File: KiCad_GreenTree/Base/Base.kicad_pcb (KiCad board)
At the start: 2 copper layers, 100 x 100 mm, 23 parts, among them Q1 BCX56, Q2 BCX56, Q3 BCX56, Q4 BCX56, SW1 SW_DPDT_x2, U1 NE555D, U2 NE555D, U3 74HC04, U4 74HC04

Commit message: Verbindung zu Baum
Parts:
- removed U4: 74HC04, Package_SO:SOIC-14W_7.5x9mm_P1.27mm
- added REF**: Verbindung_Basis, Bib:Verbindung_Basis, F.Cu at (137.1, 92.4)
- C1: footprint Capacitor_SMD:C_01005_0402Metric -> Capacitor_SMD:C_1206_3216Metric_Pad1.33x1.80mm_HandSolder
- C2, C3, C4: footprint Capacitor_SMD:C_01005_0402Metric_Pad0.57x0.30mm_HandSolder -> Capacitor_SMD:C_1206_3216Metric_Pad1.33x1.80mm_HandSolder
- R1, R2, R3, R4, R5, R6: footprint Resistor_SMD:R_01005_0402Metric_Pad0.57x0.30mm_HandSolder -> Resistor_SMD:R_1206_3216Metric_Pad1.30x1.75mm_HandSolder
- moved C3 28.0 mm to (71.1, 85.5)
- moved C4 28.0 mm to (68.5, 85.5)
- moved R1 28.0 mm to (74.3, 85.9)
- moved R2 28.0 mm to (65.9, 84.2)
- moved R4 28.0 mm to (73.7, 84.2)
- moved R5 28.0 mm to (76.3, 84.2)
- moved R6 28.0 mm to (76.9, 85.9)
- moved C2 28.0 mm to (68.5, 83.8)
- moved R3 28.0 mm to (71.1, 83.8)
- moved U1 25.0 mm to (45.0, 70.4)
- moved BT1 19.2 mm to (183.4, 103.3)
- moved BT4 19.2 mm to (125.0, 139.3)
- moved C1 18.6 mm to (66.3, 78.7)
- moved U3 18.3 mm to (55.6, 121.9)
- moved Q2 15.2 mm to (37.8, 105.9)
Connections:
- U3 pad 3: (no net) -> Net-(Q2-Pad1)
- U3 pad 4: (no net) -> Net-(Q4-Pad1)
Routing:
- net Net-(BT1-Pad1): track 19.6 -> 0.00 mm
- net Net-(BT1-Pad2): track 19.9 -> 0.31 mm
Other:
- board text added: "+"
- board text added: "-"

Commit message: NE555 Layout
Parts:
- added C5: 100n, Capacitor_SMD:C_1206_3216Metric_Pad1.33x1.80mm_HandSolder, B.Cu at (58.9, 65.3)
- added C6: 100n, Capacitor_SMD:C_1206_3216Metric_Pad1.33x1.80mm_HandSolder, B.Cu at (59.4, 76.7)
- SW1: footprint Button_Switch_THT:SW_E-Switch_EG2219_DPDT_Angled -> Bib:Schiebeschalter
- moved SW1 81.6 mm to (173.5, 66.8), turned to 90 degrees
- moved BT3 78.2 mm to (107.2, 64.0), turned to 0 degrees
- moved BT1 77.7 mm to (106.9, 116.8), turned to 0 degrees
- moved BT4 44.2 mm to (165.1, 120.9), turned to 180 degrees
- moved U3 43.0 mm to (95.8, 106.4), turned to 270 degrees
- moved BT2 42.1 mm to (165.3, 67.8), turned to 180 degrees
- moved Q2 38.4 mm to (75.9, 101.1), turned to 270 degrees
- moved U2 37.0 mm to (58.7, 69.6), turned to 180 degrees
- moved R4 28.3 mm to (51.1, 67.3), turned to 270 degrees
- moved Q4 27.3 mm to (81.5, 101.1), turned to 270 degrees
- moved R6 26.4 mm to (70.9, 111.5), turned to 180 degrees
- moved R3 24.0 mm to (53.6, 67.3), turned to 270 degrees
- moved Q1 23.6 mm to (76.5, 113.0), turned to 270 degrees
- moved R1 21.9 mm to (53.6, 78.7), turned to 270 degrees
- moved C4 21.2 mm to (51.1, 73.4), turned to 270 degrees
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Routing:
- net GND: track 0.00 -> 38.8 mm
- net Net-(BT1-Pad1): track 0.00 -> 32.8 mm
- net Net-(BT1-Pad2): track 0.31 -> 20.4 mm
- net Net-(C4-Pad1): track 0.00 -> 13.5 mm
- net Net-(C3-Pad1): track 0.00 -> 13.5 mm
- net VCC: track 0.00 -> 12.1 mm
- net Net-(BT3-Pad1): track 0.00 -> 11.6 mm
- net Net-(R3-Pad2): track 0.00 -> 7.71 mm
- net Net-(R1-Pad2): track 0.00 -> 7.65 mm
- net Net-(C1-Pad1): track 0.00 -> 2.90 mm
- net Net-(BT2-Pad1): track 18.3 -> 20.2 mm
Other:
- board text removed: "+"
- board text removed: "-"

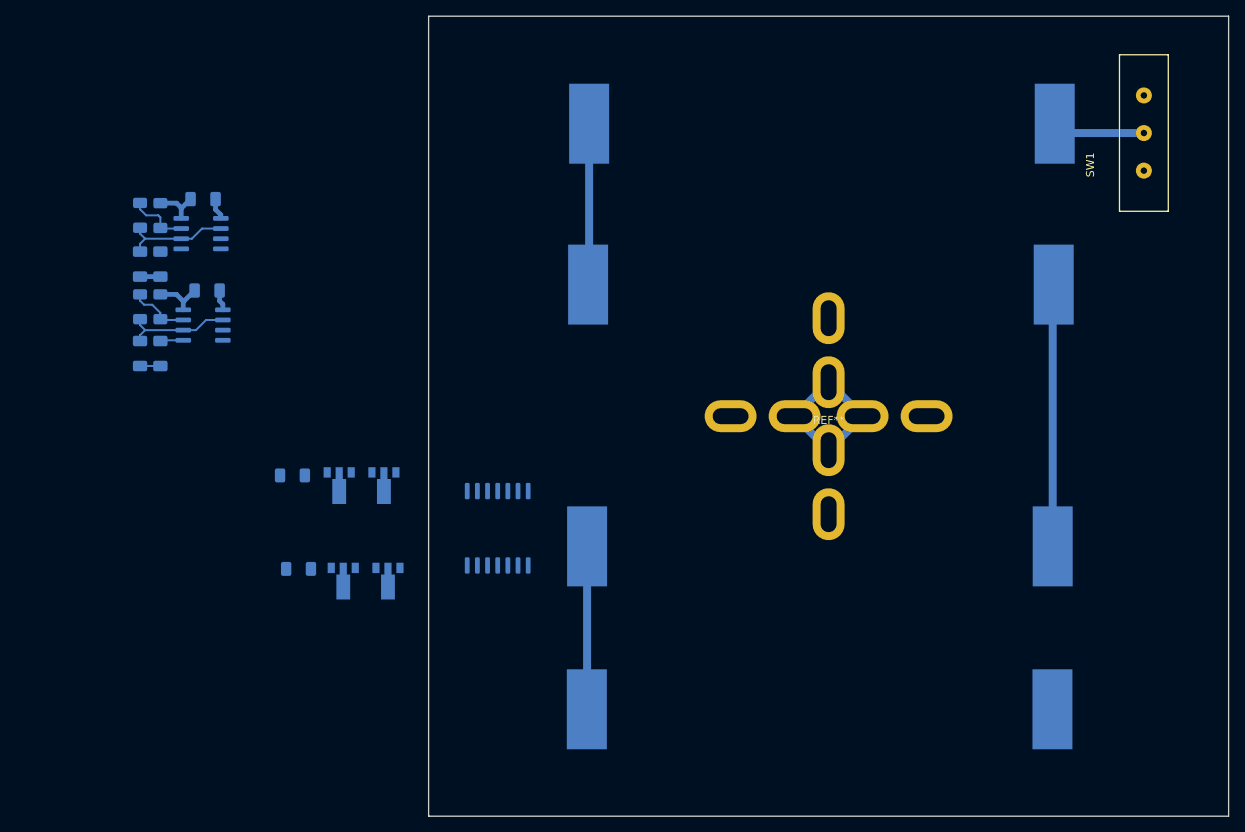
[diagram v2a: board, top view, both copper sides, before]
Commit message: Without GND
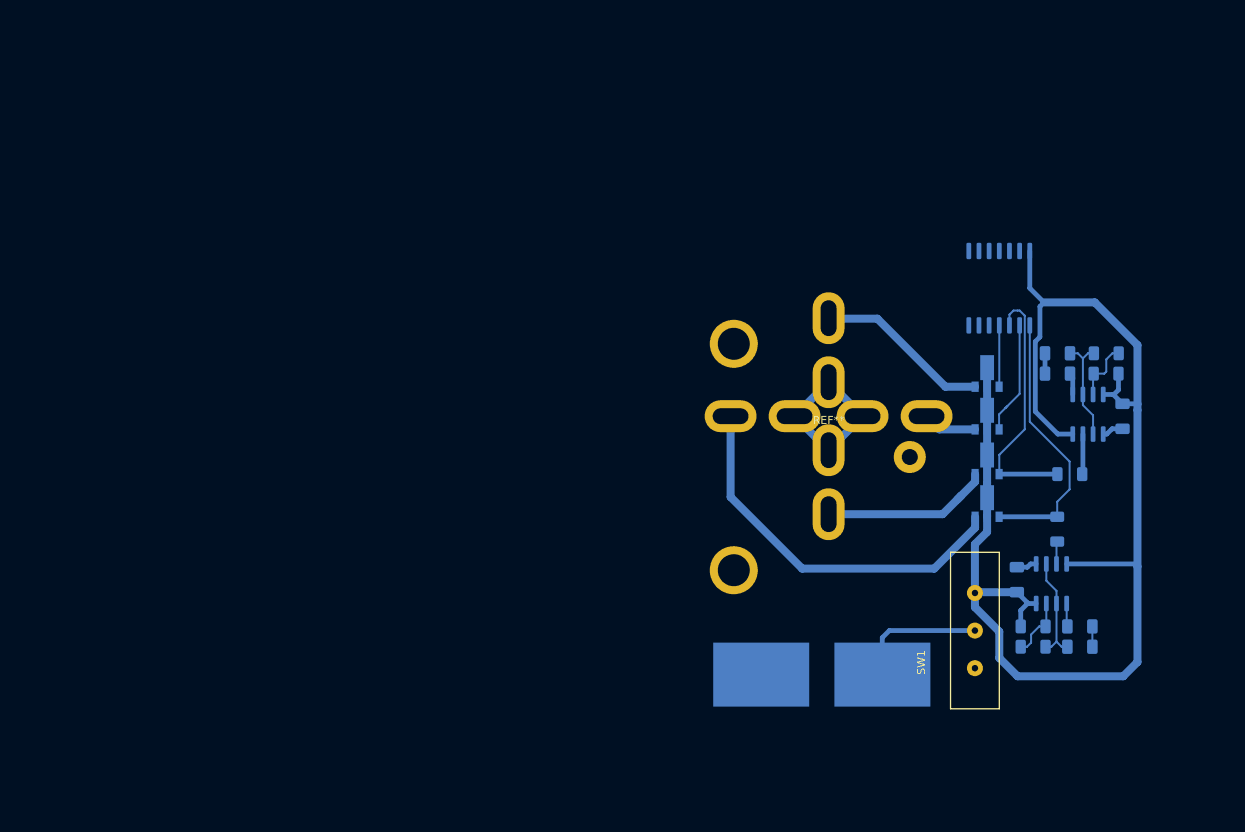
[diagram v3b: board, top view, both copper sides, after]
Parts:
- removed BT1, BT2, BT4: 1.5, Bib:Batteriehalter_für_1_Mignonzelle(AA)
- BT3: value 1.5 -> 9V; footprint Bib:Batteriehalter_für_1_Mignonzelle(AA) -> Bib:9V_Holder
- moved C3 123.1 mm to (168.5, 121.2), turned to 0 degrees
- moved R4 122.0 mm to (171.8, 84.6), turned to 180 degrees
- moved C1 119.9 mm to (168.5, 118.7), turned to 0 degrees
- moved R3 119.9 mm to (171.8, 87.1), turned to 180 degrees
- moved R2 119.4 mm to (162.7, 121.2), turned to 0 degrees
- moved C5 118.1 mm to (173.9, 92.4), turned to 270 degrees
- moved R1 116.2 mm to (162.7, 118.7), turned to 0 degrees
- moved C4 115.2 mm to (165.7, 84.6), turned to 180 degrees
- moved U2 113.1 mm to (169.5, 92.2), turned to 90 degrees
- moved C2 113.0 mm to (165.7, 87.1), turned to 180 degrees
- moved U1 110.9 mm to (165.0, 113.4), turned to 270 degrees
- moved C6 107.5 mm to (160.7, 112.9), turned to 90 degrees
- moved R5 97.2 mm to (167.3, 99.7), turned to 0 degrees
- moved R6 95.0 mm to (165.7, 106.5), turned to 270 degrees
- moved Q1 81.1 mm to (156.9, 103.3), turned to 90 degrees
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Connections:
- BT3 pad 2: Net-(BT2-Pad1) -> GND
- REF** pad 2: (no net) -> /LED_MATRIX_4
- REF** pad 4: (no net) -> /LED_MATRIX_2
- REF** pad 6: (no net) -> /LED_MATRIX_3
- REF** pad 8: (no net) -> /LED_MATRIX_1
- U3 pad 14: (no net) -> VCC
- U3 pad 7: (no net) -> GND
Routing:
- net VCC: track 12.1 -> 166.5 mm
- net /LED_MATRIX_1: track 0.00 -> 47.9 mm
- net Net-(Q1-Pad1): track 0.00 -> 33.7 mm
- net Net-(BT1-Pad1): track 32.8 -> 0.00 mm
- net Net-(Q2-Pad1): track 0.00 -> 32.0 mm
- net /LED_MATRIX_4: track 0.00 -> 21.8 mm
- net /LED_MATRIX_3: track 0.00 -> 21.6 mm
- net Net-(BT1-Pad2): track 20.4 -> 0.00 mm
- net Net-(BT2-Pad1): track 20.2 -> 0.00 mm
- net Net-(Q3-Pad1): track 0.00 -> 14.4 mm
- net Net-(Q4-Pad1): track 0.00 -> 7.80 mm
- net /LED_MATRIX_2: track 0.00 -> 6.78 mm
- net Net-(R5-Pad2): track 0.00 -> 5.04 mm
- net Net-(BT3-Pad1): track 11.6 -> 16.6 mm
- net GND: track 38.8 -> 34.4 mm
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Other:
- board outline removed
- net class VCC: clearance 0.4 -> 0.25

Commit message: Entwurf1
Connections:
- REF** pad 4: /LED_MATRIX_2 -> /LED_MATRIX_3
- REF** pad 6: /LED_MATRIX_3 -> /LED_MATRIX_2
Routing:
- net GND: track 34.4 -> 217.7 mm, vias 0 -> 6
- net /LED_MATRIX_2: track 6.78 -> 31.7 mm
- net /LED_MATRIX_3: track 21.6 -> 11.3 mm
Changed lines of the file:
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@@
     (thickness 1.6)
     (drawings 0)
-    (tracks 131)
+    (tracks 188)
     (zones 0)
     (modules 22)
@@
     )
     (pad 6 thru_hole oval (at 0 12.25) (size 4 6.5) (drill oval 2 4.5) (layers *.Cu *.Mask)
-      (net 10 /LED_MATRIX_3))
+      (net 12 /LED_MATRIX_2))
     (pad 5 thru_hole oval (at 0 4.25) (size 4 6.5) (drill oval 2 4.5) (layers *.Cu *.Mask)
       (net 2 GND))
@@
       (net 2 GND))
     (pad 4 thru_hole oval (at 12.25 0) (size 6.5 4) (drill oval 4.5 2) (layers *.Cu *.Mask)
-      (net 12 /LED_MATRIX_2))
+      (net 10 /LED_MATRIX_3))
     (pad 3 thru_hole oval (at 4.25 0) (size 6.5 4) (drill oval 4.5 2) (layers *.Cu *.Mask)
       (net 2 GND))
@@
   (segment (start 172.5547 93.9931) (end 173.8632 93.9931) (width 0.6) (layer B.Cu) (net 2))
   (segment (start 171.8962 94.6516) (end 172.5547 93.9931) (width 0.6) (layer B.Cu) (net 2))
+  (segment (start 170.0915 118.6944) (end 170.0915 114.4655) (width 1) (layer B.Cu) (net 2))
+  (via (at 166.586 112.992) (size 0.8) (drill 0.4) (layers F.Cu B.Cu) (net 2))
+  (segment (start 168.618 112.992) (end 166.586 112.992) (width 1) (layer B.Cu) (net 2))
+  (segment (start 170.0915 114.4655) (end 168.618 112.992) (width 1) (layer B.Cu) (net 2))
+  (via (at 163.284 112.992) (size 0.8) (drill 0.4) (layers F.Cu B.Cu) (net 2))
+  (segment (start 166.586 112.992) (end 163.284 112.992) (width 1) (layer F.Cu) (net 2))
+  (segment (start 163.284 112.992) (end 162.522 112.992) (width 1) (layer B.Cu) (net 2))
+  (segment (start 162.522 112.992) (end 160.998 111.468) (width 1) (layer B.Cu) (net 2))
+  (segment (start 160.655 107.747) (end 162.014 106.388) (width 1) (layer B.Cu) (net 2))
+  (segment (start 160.655 111.2899) (end 160.655 107.747) (width 1) (layer B.Cu) (net 2))
+  (segment (start 173.952 100.292) (end 173.952 93.942) (width 1) (layer B.Cu) (net 2))
+  (via (at 171.412 92.418) (size 0.8) (drill 0.4) (layers F.Cu B.Cu) (net 2))
+  (segment (start 171.4502 92.4562) (end 171.412 92.418) (width 1) (layer B.Cu) (net 2))
+  (segment (start 171.4502 94.6516) (end 171.4502 92.4562) (width 1) (layer B.Cu) (net 2))
+  (via (at 168.11 92.418) (size 0.8) (drill 0.4) (layers F.Cu B.Cu) (net 2))
+  (segment (start 171.412 92.418) (end 168.11 92.418) (width 1) (layer F.Cu) (net 2))
+  (segment (start 168.11 92.418) (end 164.046 88.354) (width 1) (layer B.Cu) (net 2))
+  (segment (start 164.046 87.592) (end 164.3 87.338) (width 1) (layer B.Cu) (net 2))
+  (segment (start 164.046 88.354) (end 164.046 87.592) (width 1) (layer B.Cu) (net 2))
+  (segment (start 165.57 83.1593) (end 165.57 79.972) (width 1) (layer B.Cu) (net 2))
+  (segment (start 164.1727 84.5566) (end 165.57 83.1593) (width 1) (layer B.Cu) (net 2))
+  (segment (start 154.648 81.066) (end 154.648 79.914315) (width 1) (layer B.Cu) (net 2))
+  (segment (start 154.648 79.914315) (end 154.590315 79.914315) (width 1) (layer B.Cu) (net 2))
+  (segment (start 154.590315 79.914315) (end 149.568 74.892) (width 1) (layer B.Cu) (net 2))
+  (segment (start 149.568 74.892) (end 137.32961 74.892) (width 1) (layer B.Cu) (net 2))
+  (segment (start 137.32961 74.892) (end 134.328 74.892) (width 1) (layer B.Cu) (net 2))
+  (segment (start 134.328 74.892) (end 130.772 78.448) (width 1) (layer B.Cu) (net 2))
+  (segment (start 130.772 78.448) (end 130.772 82.004) (width 1) (layer B.Cu) (net 2))
+  (segment (start 130.772 82.004) (end 137.122 88.354) (width 1) (layer B.Cu) (net 2))
+  (segment (start 128.695 124.72) (end 128.95 124.72) (width 1) (layer B.Cu) (net 2))
+  (segment (start 128.95 124.72) (end 131.28 122.39) (width 1) (layer B.Cu) (net 2))
+  (segment (start 131.28 112.203998) (end 123.152 104.075998) (width 1) (layer B.Cu) (net 2))
+  (segment (start 131.28 122.39) (end 131.28 112.203998) (width 1) (layer B.Cu) (net 2))
+  (segment (start 120.92199 91.29962) (end 123.86761 88.354) (width 1) (layer B.Cu) (net 2))
+  (segment (start 120.92199 101.845988) (end 120.92199 91.29962) (width 1) (layer B.Cu) (net 2))
+  (segment (start 123.152 104.075998) (end 120.92199 101.845988) (width 1) (layer B.Cu) (net 2))
+  (segment (start 123.86761 88.354) (end 136.868 88.354) (width 1) (layer B.Cu) (net 2))
+  (segment (start 167.856 106.388) (end 173.952 100.292) (width 1) (layer B.Cu) (net 2))
+  (segment (start 162.014 106.388) (end 167.856 106.388) (width 1) (layer B.Cu) (net 2))
+  (via (at 165.57 79.464) (size 0.8) (drill 0.4) (layers F.Cu B.Cu) (net 2))
+  (segment (start 165.57 79.972) (end 165.57 79.464) (width 1) (layer B.Cu) (net 2))
+  (via (at 165.57 76.924) (size 0.8) (drill 0.4) (layers F.Cu B.Cu) (net 2))
+  (segment (start 165.57 79.464) (end 165.57 76.924) (width 1) (layer F.Cu) (net 2))
+  (segment (start 149.568 74.618902) (end 149.568 74.892) (width 1) (layer B.Cu) (net 2))
+  (segment (start 154.374902 69.812) (end 149.568 74.618902) (width 1) (layer B.Cu) (net 2))
+  (segment (start 164.3 69.812) (end 154.374902 69.812) (width 1) (layer B.Cu) (net 2))
+  (segment (start 165.57 71.082) (end 164.3 69.812) (width 1) (layer B.Cu) (net 2))
+  (segment (start 165.57 76.924) (end 165.57 71.082) (width 1) (layer B.Cu) (net 2))
   (segment (start 166.878 118.6059) (end 166.9665 118.6944) (width 0.25) (layer B.Cu) (net 3))
   (segment (start 166.878 115.8354) (end 166.878 118.6059) (width 0.25) (layer B.Cu) (net 3))
@@
   (segment (start 162.268 93.1038) (end 167.2464 98.0822) (width 0.25) (layer B.Cu) (net 9))
   (segment (start 162.268 81.066) (end 162.268 93.1038) (width 0.25) (layer B.Cu) (net 9))
-  (segment (start 155.434 99.656) (end 155.434 100.612824) (width 1) (layer B.Cu) (net 10))
-  (segment (start 151.378824 104.668) (end 153.677412 102.369412) (width 1) (layer B.Cu) (net 10))
-  (segment (start 137.122 104.668) (end 151.378824 104.668) (width 1) (layer B.Cu) (net 10))
-  (segment (start 153.677412 102.369412) (end 153.214824 102.832) (width 1) (layer B.Cu) (net 10))
-  (segment (start 155.434 100.612824) (end 153.677412 102.369412) (width 1) (layer B.Cu) (net 10))
   (segment (start 158.434 99.656) (end 165.4928 99.656) (width 0.6) (layer B.Cu) (net 11))
   (segment (start 159.728 81.066) (end 159.728 79.718) (width 0.25) (layer B.Cu) (net 11))
@@
   (segment (start 161.64299 94.05901) (end 158.458 97.244) (width 0.25) (layer B.Cu) (net 11))
   (segment (start 158.458 97.244) (end 158.458 99.784) (width 0.25) (layer B.Cu) (net 11))
-  (segment (start 155.434 94.068) (end 150.964 94.068) (width 1) (layer B.Cu) (net 12))
-  (segment (start 149.372 92.476) (end 150.964 94.068) (width 1) (layer B.Cu) (net 12))
-  (segment (start 149.372 92.418) (end 149.372 92.476) (width 1) (layer B.Cu) (net 12))
+  (segment (start 149.372 92.418) (end 149.372 92.476) (width 1) (layer B.Cu) (net 10))
+  (segment (start 155.434 99.656) (end 152.996 99.656) (width 1) (layer B.Cu) (net 10))
+  (segment (start 152.996 99.656) (end 149.822 96.482) (width 1) (layer B.Cu) (net 10))
+  (segment (start 149.822 96.482) (end 149.822 94.704) (width 1) (layer B.Cu) (net 10))
+  (segment (start 149.822 94.704) (end 149.822 92.164) (width 1) (layer B.Cu) (net 10))
+  (segment (start 137.122 104.668) (end 139.35 104.668) (width 1) (layer B.Cu) (net 12))
+  (segment (start 139.35 104.668) (end 140.62 104.668) (width 1) (layer B.Cu) (net 12))
+  (segment (start 140.62 104.668) (end 143.726 101.562) (width 1) (layer B.Cu) (net 12))
+  (segment (start 143.726 97.067998) (end 143.726 101.562) (width 1) (layer B.Cu) (net 12))
+  (segment (start 145.32201 95.471988) (end 143.726 97.067998) (width 1) (layer B.Cu) (net 12))
+  (segment (start 145.32201 91.32999) (end 145.32201 95.471988) (width 1) (layer B.Cu) (net 12))
+  (segment (start 146.93401 89.71799) (end 145.32201 91.32999) (width 1) (layer B.Cu) (net 12))
+  (segment (start 151.74038 89.71799) (end 146.93401 89.71799) (width 1) (layer B.Cu) (net 12))
+  (segment (start 153.32201 91.29962) (end 151.74038 89.71799) (width 1) (layer B.Cu) (net 12))
+  (segment (start 153.32201 91.95601) (end 153.32201 91.29962) (width 1) (layer B.Cu) (net 12))
+  (segment (start 155.434 94.068) (end 153.32201 91.95601) (width 1) (layer B.Cu) (net 12))
   (segment (start 158.434 94.068) (end 158.434 92.188) (width 0.25) (layer B.Cu) (net 13))
   (segment (start 158.434 92.188) (end 159.22 91.402) (width 0.25) (layer B.Cu) (net 13))
@@
   (segment (start 160.998 81.066) (end 160.998 89.624) (width 0.25) (layer B.Cu) (net 13))
   (segment (start 159.22 91.402) (end 159.474 91.148) (width 0.25) (layer B.Cu) (net 13))
-  (segment (start 155.434 88.734) (end 151.726 88.734) (width 1) (layer B.Cu) (net 14))
-  (segment (start 151.726 88.734) (end 143.218 80.226) (width 1) (layer B.Cu) (net 14))
   (segment (start 143.218 80.226) (end 137.122 80.226) (width 1) (layer B.Cu) (net 14))
+  (segment (start 155.434 88.734) (end 153.25 88.734) (width 1) (layer B.Cu) (net 14))
+  (segment (start 144.742 80.226) (end 143.218 80.226) (width 1) (layer B.Cu) (net 14))
+  (segment (start 153.25 88.734) (end 144.742 80.226) (width 1) (layer B.Cu) (net 14))
   (segment (start 158.458 81.066) (end 158.458 88.862) (width 0.25) (layer B.Cu) (net 15))
   (segment (start 164.237 118.6944) (end 163.449 118.6944) (width 0.25) (layer B.Cu) (net 16))

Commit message: update
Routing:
- added copper zone on B.Cu, net GND
- added copper zone on F.Cu, net GND
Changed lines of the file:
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@@
       (effects (font (size 1 1) (thickness 0.15)) (justify mirror))
     )
-    (fp_text value 9V (at 27.325 1.425 90) (layer B.Fab)
+    (fp_text value 9V (at 27.432 -1.27 90) (layer B.Fab)
       (effects (font (size 1 1) (thickness 0.15)) (justify mirror))
     )
@@
   (segment (start 168.9102 94.6516) (end 168.9102 99.695) (width 0.6) (layer B.Cu) (net 18))
   (segment (start 165.608 110.8854) (end 165.608 108.1534) (width 0.25) (layer B.Cu) (net 19))
+  (zone (net 2) (net_name GND) (layer B.Cu) (hatch edge 0.508)
+    (connect_pads (clearance 0.508))
+    (min_thickness 0.254)
+    (fill yes (arc_segments 32) (thermal_gap 0.508) (thermal_bridge_width 0.508))
+    (polygon
+      (pts
+        (xy 176.746 129.248) (xy 119.85 129.248) (xy 119.85 69.05) (xy 176.746 69.05)
+      )
+    )
+  )
+  (zone (net 2) (net_name GND) (layer F.Cu) (hatch edge 0.508)
+    (connect_pads (clearance 0.508))
+    (min_thickness 0.254)
+    (fill yes (arc_segments 32) (thermal_gap 0.508) (thermal_bridge_width 0.508))
+    (polygon
+      (pts
+        (xy 176.746 129.248) (xy 119.85 129.248) (xy 119.85 69.05) (xy 176.746 69.05)
+      )
+    )
+  )
 )
